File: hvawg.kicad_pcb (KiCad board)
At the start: 2 copper layers, 150 x 40 mm, 90 parts, among them J1 Conn_01x04_Pin, J10 Conn_01x01_Pin, J2 Conn_01x04_Pin, J3 Conn_01x04_Pin, J4 Conn_01x04_Pin, J5 Conn_01x04_Pin, J6 Conn_01x04_Pin, J7 Conn_01x04_Pin, J8 Conn_01x04_Pin, J9 Conn_01x08_Pin, Q1 IRF730, Q3 IRF9610, U1 L7805, U2 74HC595D,110, U3 DAC0808LCMX/NOPB, U4 NE5532, U6 LM8261, U7 LM8261, U8 NE5532

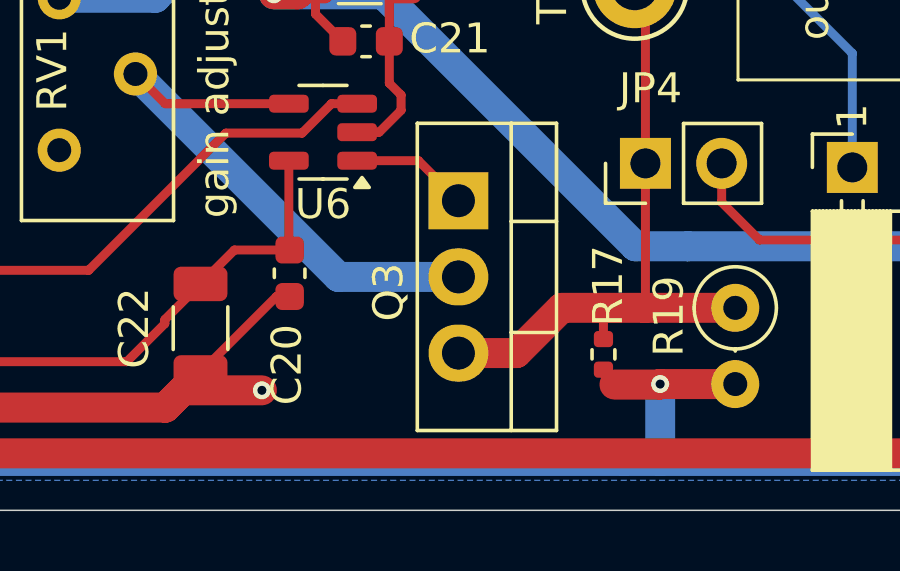
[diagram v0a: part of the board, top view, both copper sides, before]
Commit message: Fix Q3 source/drain swap in design files; regenerate gerbers
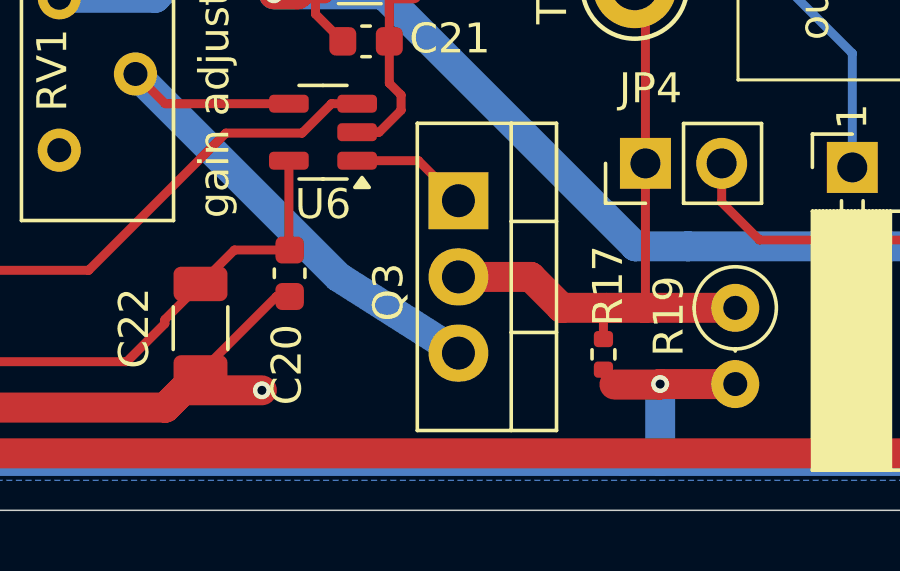
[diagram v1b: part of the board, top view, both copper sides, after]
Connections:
- Q3 pad 2: Net-(Q3-D) -> levelshift_out
- Q3 pad 3: levelshift_out -> Net-(Q3-S)
- RV1 pad 2: Net-(Q3-D) -> Net-(Q3-S)
- U6 pad 4: Net-(Q3-D) -> Net-(Q3-S)
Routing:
- net Net-(Q3-S): track 0.00 -> 19.8 mm
- net Net-(Q3-D): track 19.1 -> 0.00 mm

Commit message: new board
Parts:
- removed J10: Conn_01x01_Pin, Connector_PinSocket_2.54mm:PinSocket_1x01_P2.54mm_Horizontal
- added C32: DNP, Capacitor_SMD:C_1206_3216Metric, F.Cu at (209.3, 89.8)
- added D4: BZT52C12, Diode_SMD:D_SOD-123, F.Cu at (273.8, 108.2)
- added D5: BZT52C12, Diode_SMD:D_SOD-123, F.Cu at (166.3, 120.2)
- added HS1: Wakefield 272-AB, Library:Heatsink_Wakefield_272-AB, F.Cu at (232.5, 104.0)
- added R26: 3.3k, Resistor_SMD:R_0402_1005Metric, F.Cu at (161.6, 107.9)
- added R27: 820, Resistor_SMD:R_0402_1005Metric, F.Cu at (161.6, 97.0)
- added R28: 100k, Resistor_SMD:R_0402_1005Metric, F.Cu at (277.3, 105.0)
- added R29: 1M, Resistor_SMD:R_0402_1005Metric, F.Cu at (166.3, 117.0)
- added R30: 22k, Resistor_SMD:R_2512_6332Metric, F.Cu at (162.2, 89.9)
- added R31: 4.7k, Resistor_SMD:R_2512_6332Metric, F.Cu at (196.7, 92.5)
- added R32: DNP, Resistor_SMD:R_1206_3216Metric, F.Cu at (205.2, 90.3)
- added TP10: TestPoint, TestPoint:TestPoint_Pad_D1.5mm, F.Cu at (276.6, 112.9)
- added TP11: TestPoint, TestPoint:TestPoint_Pad_D1.5mm, F.Cu at (270.8, 100.6)
- added TP12: TestPoint, TestPoint:TestPoint_Pad_D1.5mm, F.Cu at (266.1, 108.8)
- added TP6: TestPoint, TestPoint:TestPoint_Keystone_5005-5009_Compact, F.Cu at (190.3, 99.3)
- added TP7: TestPoint, TestPoint:TestPoint_Keystone_5005-5009_Compact, F.Cu at (171.0, 109.5)
- added TP8: TestPoint, TestPoint:TestPoint_Keystone_5005-5009_Compact, F.Cu at (151.5, 111.0)
- added TP9: TestPoint, TestPoint:TestPoint_Pad_D1.5mm, F.Cu at (276.7, 95.8)
- J7: value Conn_01x04_Pin -> Conn_01x07_Pin; footprint Library:PinSocket_1x04_P2.54mm_Horizontal_flipped -> Library:PinSocket_1x07_P2.54mm_Horizontal_flipped
- J8: value Conn_01x04_Pin -> Conn_01x07_Pin; footprint Connector_PinSocket_2.54mm:PinSocket_1x04_P2.54mm_Horizontal -> Connector_PinSocket_2.54mm:PinSocket_1x07_P2.54mm_Horizontal
- J9: footprint Connector_PinHeader_2.54mm:PinHeader_1x08_P2.54mm_Vertical -> Library:PhoenixContact_MC_1,5_8-G-3.5_1x08_P3.50mm_Horizontal_EdgeNotch
- Q1, Q3: footprint Package_TO_SOT_THT:TO-220-3_Vertical -> Library:TO-220-3_Vertical_HV
- R21: footprint Resistor_THT:R_Axial_Power_L25.0mm_W9.0mm_P10.16mm_Vertical -> Library:TO-220-2_Horizontal_LTO50
- RV1: value 3k -> 1k
- moved H3 58.0 mm to (278.0, 73.2)
- moved H4 57.6 mm to (278.0, 122.0)
- moved C24 57.5 mm to (264.1, 101.7)
- moved C25 57.5 mm to (267.8, 101.7)
- moved Q1 57.5 mm to (280.3, 102.7)
- moved R15 57.5 mm to (260.2, 101.7)
- moved U7 57.5 mm to (271.3, 103.8)
- moved R18 57.5 mm to (275.2, 103.2)
- moved R22 57.5 mm to (270.2, 110.0)
- moved R23 57.5 mm to (269.5, 115.5)
- moved J9 51.2 mm to (177.8, 76.5), turned to 180 degrees
- moved R25 45.9 mm to (152.1, 103.9), turned to 180 degrees
- moved R24 17.9 mm to (179.6, 84.0), turned to 90 degrees
- moved J7 13.2 mm to (197.9, 79.6)
- moved J5 10.9 mm to (148.4, 79.6)
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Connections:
- C14 pad 1: Net-(U8A-+) -> Net-(C14-Pad1)
- C15 pad 1: Net-(U8A-+) -> Net-(C14-Pad1)
- J5 pad 1: GND -> +100V
- J5 pad 2: +100V -> GND
- J5 pad 3: -100+12V -> -100V
- J5 pad 4: -100V -> -100+12V
- J6 pad 1: GND -> +100V
- J6 pad 2: +100V -> GND
- J6 pad 3: -100+12V -> -100V
- J6 pad 4: -100V -> -100+12V
- J7 pad 2: Net-(J7-Pin_2) -> GND
- J7 pad 4: Net-(J7-Pin_4) -> GND
- J8 pad 2: Net-(J7-Pin_2) -> GND
- J8 pad 4: Net-(J7-Pin_4) -> GND
- J9 pad 2: GND -> +12V
- J9 pad 3: +12V -> -12V
- J9 pad 4: -12V -> GND
- J9 pad 5: GND -> +100V
- J9 pad 6: +100V -> GND
- J9 pad 7: -100+12V -> -100V
- J9 pad 8: -100V -> -100+12V
- JP10 pad 1: Net-(JP10-A) -> output_post
- JP10 pad 2: Net-(J7-Pin_3) -> Net-(J7-Pin_5)
- JP11 pad 1: Net-(JP10-A) -> output_post
- JP11 pad 2: Net-(J7-Pin_4) -> Net-(J7-Pin_7)
- JP8 pad 1: Net-(JP10-A) -> output_post
- JP9 pad 1: Net-(JP10-A) -> output_post
- JP9 pad 2: Net-(J7-Pin_2) -> Net-(J7-Pin_3)
- Q1 pad 2: Net-(JP10-A) -> Net-(Q1-D)
- Q3 pad 3: Net-(Q3-S) -> Net-(D5-K)
- R12 pad 2: Net-(U8A-+) -> Net-(C14-Pad1)
- R21 pad 1: Net-(JP10-A) -> Net-(Q1-D)
- RV1 pad 1: Net-(JP6-A) -> Net-(R26-Pad2)
- RV1 pad 2: Net-(Q3-S) -> Net-(D5-K)
- RV1 pad 3: unconnected-(RV1-Pad3) -> Net-(D5-K)
- RV2 pad 1: Net-(U8A-+) -> Net-(C14-Pad1)
- RV2 pad 2: GND -> Net-(R27-Pad1)
- RV2 pad 3: unconnected-(RV2-Pad3) -> Net-(R27-Pad1)
- TP5 pad 1: Net-(JP10-A) -> Net-(Q1-D)
- U4 pad 5: (no net) -> GND
- U4 pad 6: (no net) -> Net-(U4B--)
- U4 pad 7: (no net) -> Net-(U4B--)
- U6 pad 4: Net-(Q3-S) -> Net-(D5-K)
- U8 pad 5: (no net) -> GND
- U8 pad 6: (no net) -> Net-(U8B--)
- U8 pad 7: (no net) -> Net-(U8B--)
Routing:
- net GND: track 529.9 -> 257.3 mm, vias 12 -> 23
- net Net-(Q1-D): track 0.00 -> 115.3 mm, vias 0 -> 1
- net -100V: track 138.5 -> 248.5 mm, vias 6 -> 5
- net -100+12V: track 110.7 -> 210.5 mm, vias 4 -> 1
- net Net-(JP4-B): track 38.3 -> 112.1 mm, vias 0 -> 1
- net +100V: track 112.5 -> 185.3 mm, vias 2 -> 3
- net Net-(JP10-A): track 67.3 -> 0.00 mm
- net -12V: track 138.7 -> 192.4 mm, vias 5 -> 3
- net Net-(J7-Pin_5): track 0.00 -> 40.8 mm
- net Net-(J7-Pin_7): track 0.00 -> 40.7 mm
- net Net-(D5-K): track 0.00 -> 39.0 mm
- net output_post: track 0.00 -> 35.9 mm
- net Net-(J7-Pin_2): track 20.7 -> 0.00 mm
- net Net-(Q3-S): track 19.8 -> 0.00 mm
- net Net-(J7-Pin_4): track 19.7 -> 0.00 mm
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- added copper zone on F.Cu, net GND
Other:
- board size 150 x 40 mm -> 207 x 58.8 mm
- board text added: "- INSULATE"
- board text added: "5"
- board text added: "6"
- board text added: "7"
- board text added: "8"
- board text added: "G"
- board text added: "HIGH VOLTAGE"
- board text added: "HOT >100C"
- board text added: "HV_AWG v2"
- board text added: "Q1 TAB = OUTPUT +/-150V"
- board text added: "Q1 TAB=OUT +/-150V"
- board text added: "SINK = GND"
- board text added: "TAB ~ -150V"
- board text added: "Vhi"
- board text added: "Vlo"
- board text added: "Vlo+12"
- board text removed: "HV_AWG v1"
- board text removed: "Vhigh"
- board text removed: "Vlow"
- board text removed: "Vlow+12"
- board text removed: "out1"
- board text removed: "out2"
- board text removed: "out3"
- board text removed: "out4"

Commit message: all of the V2 changes: schematic changes, labels, regenerated gerbers, etc
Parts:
- R1, R10, R11, R17, R2, R3, R4, R5, R6, R7, R8, R9: value 2.7k -> 2.74k
- U1: value L7805 -> L78M05ABDT-TR
- U2: value 74HC595D,110 -> 74HCT595D,118
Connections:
- net Net-(JP1-B) renamed +5V
